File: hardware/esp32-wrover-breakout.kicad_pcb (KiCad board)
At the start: 2 copper layers, 25.4 x 36.2 mm, 10 parts, among them IC1 ESP32-WROVER-E_M213EH6464PH3Q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, J1 Conn_01x04_Male, J2 Conn_01x10_Male, J3 Conn_01x10_Male, Q1 MUN5214DW1T1G, U1 XC6220B331MR

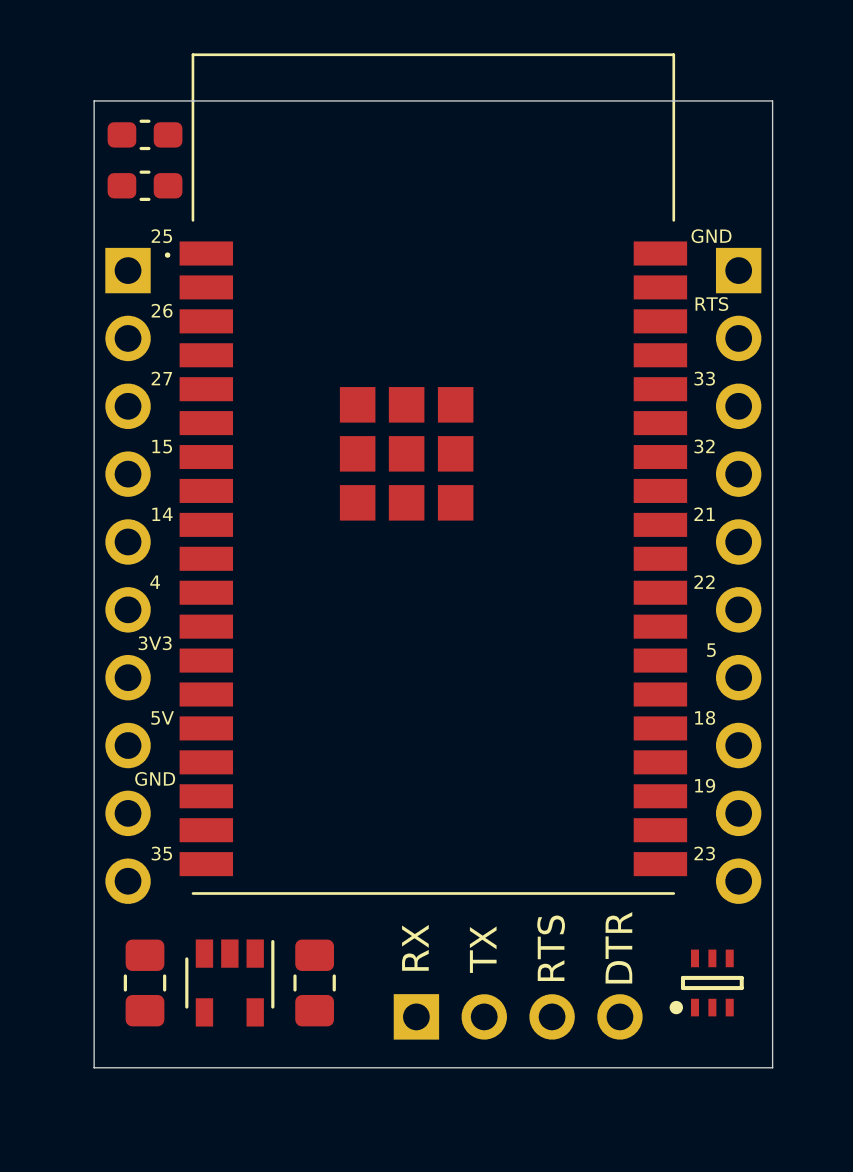
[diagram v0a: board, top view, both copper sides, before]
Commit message: First routing done
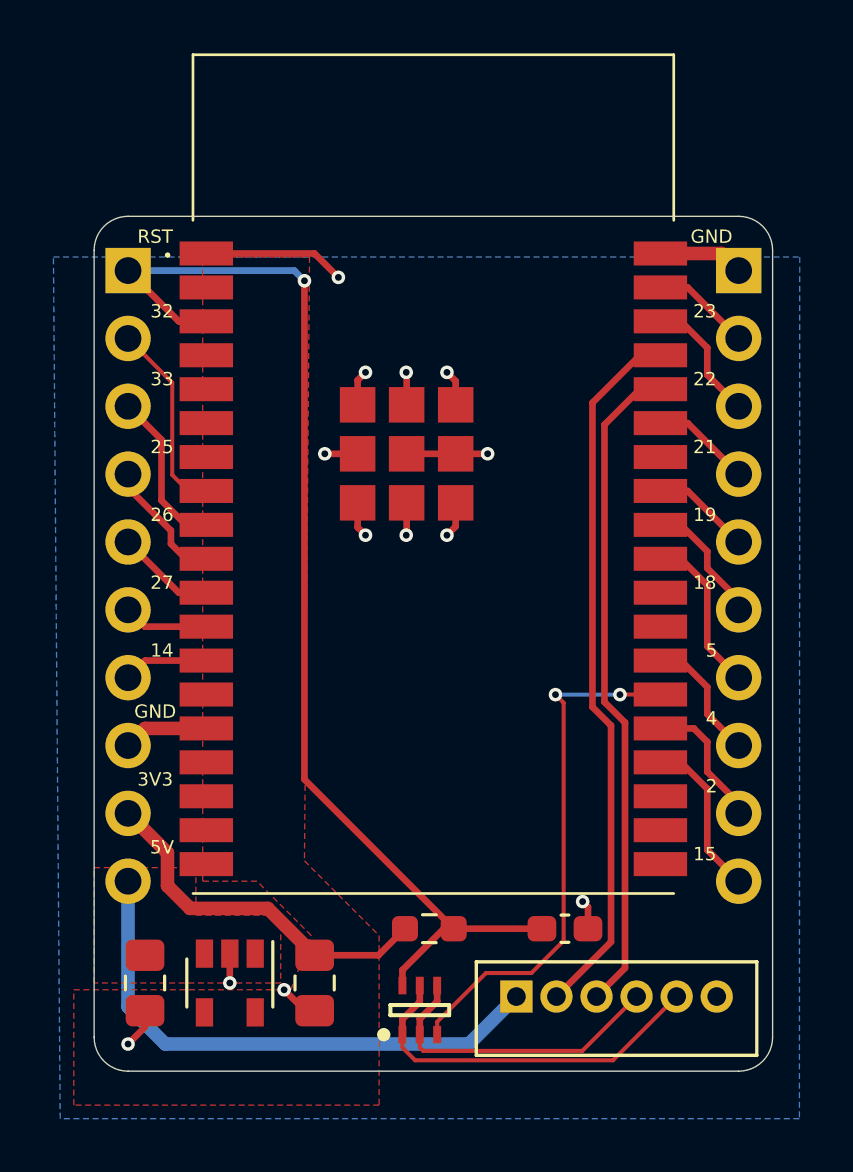
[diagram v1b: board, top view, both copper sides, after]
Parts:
- removed C2: 0.1uF, Capacitor_SMD:C_0603_1608Metric_Pad1.08x0.95mm_HandSolder
- added R1: 10k, Resistor_SMD:R_0603_1608Metric_Pad0.98x0.95mm_HandSolder, F.Cu at (49.9, 60.5)
- J1: value Conn_01x04_Male -> Conn_01x06_Male; footprint Connector_PinHeader_2.54mm:PinHeader_1x04_P2.54mm_Vertical -> B6B-ZR(LF)(SN):JST_B6B-ZR(LF)(SN)
- moved C3 31.9 mm to (55.0, 60.5), turned to 0 degrees
- moved Q1 11.0 mm to (49.5, 63.5)
- moved J1 7.53 mm to (56.9, 63.0), turned to 180 degrees
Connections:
- IC1 pad 15: Net-(IC1-Pad15) -> GND
- IC1 pad 24: Net-(IC1-Pad24) -> /GPIO2
- IC1 pad 7: /GPIO35 -> Net-(IC1-Pad7)
- J1 pad 1: /RX -> +5V
- J1 pad 3: /RTS -> /RX
- J2 pad 1: /GPIO25 -> /RESET
- J2 pad 10: /GPIO35 -> +5V
- J2 pad 2: /GPIO26 -> /GPIO32
- J2 pad 3: /GPIO27 -> /GPIO33
- J2 pad 4: /GPIO15 -> /GPIO25
- J2 pad 5: /GPIO14 -> /GPIO26
- J2 pad 6: /GPIO4 -> /GPIO27
- J2 pad 7: +3V3 -> /GPIO14
- J2 pad 8: +5V -> GND
- J2 pad 9: GND -> +3V3
- J3 pad 10: /GPIO23 -> /GPIO15
- J3 pad 2: /RESET -> /GPIO23
- J3 pad 3: /GPIO33 -> /GPIO22
- J3 pad 4: /GPIO32 -> /GPIO21
- J3 pad 5: /GPIO21 -> /GPIO19
- J3 pad 6: /GPIO22 -> /GPIO18
- J3 pad 8: /GPIO18 -> /GPIO4
- J3 pad 9: /GPIO19 -> /GPIO2
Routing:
- net /RESET: track 0.00 -> 43.5 mm, vias 0 -> 1
- net GND: track 0.00 -> 29.0 mm, vias 0 -> 13
- net /TX: track 0.00 -> 26.6 mm
- net /RX: track 0.00 -> 24.8 mm
- net +5V: track 0.00 -> 20.6 mm
- net /GPIO0: track 0.00 -> 19.7 mm, vias 0 -> 2
- net /RTS: track 0.00 -> 14.0 mm
- net +3V3: track 0.00 -> 13.7 mm
- net /DTR: track 0.00 -> 11.6 mm
- net /GPIO32: track 0.00 -> 7.32 mm
- net /GPIO5: track 0.00 -> 6.11 mm
- net /GPIO15: track 0.00 -> 6.11 mm
- net /GPIO33: track 0.00 -> 6.10 mm
- net /GPIO2: track 0.00 -> 5.13 mm
- net /GPIO4: track 0.00 -> 4.84 mm
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- added copper zone on F.Cu, net +3V3
- added copper zone on F.Cu, net +5V
- added copper zone on B.Cu, net GND
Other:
- board size 25.4 x 36.2 mm -> 25.4 x 32 mm
- rule trace_min: 0.2 -> 0.1524
- rule via_min_drill: 0.3 -> 0.254
- board text added: "2"
- board text added: "RST"
- board text removed: "35"
- board text removed: "DTR"
- board text removed: "RTS"
- board text removed: "RX"
- board text removed: "TX"

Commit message: Rev 1.0
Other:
- board text added: "François Gervais 29 dec 2020 rev 1.0"
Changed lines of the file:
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@@
   (general
     (thickness 1.6)
-    (drawings 28)
+    (drawings 29)
     (tracks 153)
     (zones 0)
@@
     )
   )
+  (gr_text "François Gervais\n29 dec 2020\nrev 1.0" (at 59.69 55.626) (layer B.SilkS)
+    (effects (font (size 1 1) (thickness 0.15)) (justify left mirror))
+  )
   (gr_arc (start 61.468 64.516) (end 61.468 65.786) (angle -90) (layer Edge.Cuts) (width 0.05))
